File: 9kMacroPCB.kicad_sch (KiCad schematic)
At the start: 0 parts

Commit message: PCB updates
added PCB device libs and assigned footprints
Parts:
- added D1, D2, D3, D4, D5, D6, D7, D8, D9: D_Small, Diode_SMD:D_SOD-123, symbol Device:D_Small
- added MX1, MX2, MX3, MX4, MX5, MX6, MX7, MX8, MX9: MX-NoLED, MX_Alps_Hybrid2:MX-1U-NoLED, symbol MX_Alps_Hybrid:MX-NoLED
- added R1, R2, R3, R4, R5, R6: 10k, Resistor_SMD:R_0805_2012Metric, symbol Device:R_Small
- added U1: XIAO-RP2040-SMD, Seeed Studio XIAO Series Library:XIAO-RP2040-DIP, symbol Seeed_Studio_XIAO_Series:XIAO-RP2040-SMD
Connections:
- new net: D9.2 (A), MX9.2 (ROW)
- new net: R6.2, U1.6 (GPIO7_D5_SCL)
- new net: D4.2 (A), MX8.2 (ROW)
- new net: R4.2, U1.4 (GPIO29_A3_D3)
- new net: R1.2, U1.1 (GPIO26_A0_D0)
- new net: R2.2, U1.2 (GPIO27_A1_D1)
- new net: R3.2, U1.3 (GPIO28_A2_D2)
- new net: R5.2, U1.5 (GPIO6_D4_SDA)
- new net: D7.2 (A), MX3.2 (ROW)
- new net: D2.2 (A), MX4.2 (ROW)
- new net: D1.2 (A), MX1.2 (ROW)
- new net: D8.2 (A), MX6.2 (ROW)
- new net: D3.2 (A), MX7.2 (ROW)
- new net: D6.2 (A), MX2.2 (ROW)
- new net: D5.2 (A), MX5.2 (ROW)
- new net COL0: MX1.1 (COL), MX4.1 (COL), MX7.1 (COL)
- new net COL1: MX2.1 (COL), MX5.1 (COL), MX8.1 (COL)
- new net COL2: MX3.1 (COL), MX6.1 (COL), MX9.1 (COL)
- new net ROW0: D1.1 (K), D6.1 (K), D7.1 (K)
- new net ROW1: D2.1 (K), D5.1 (K), D8.1 (K)
- new net ROW2: D3.1 (K), D4.1 (K), D9.1 (K)

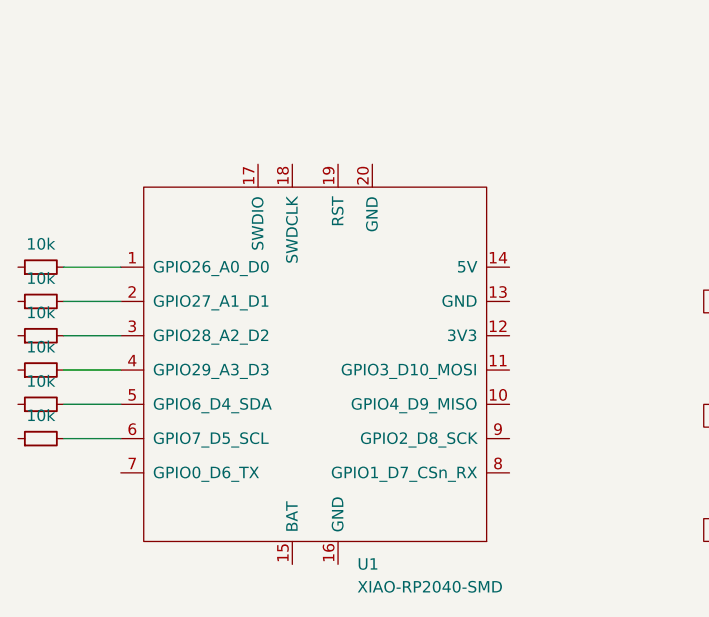
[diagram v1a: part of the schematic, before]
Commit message: Remove OPL library, add XIAO RP2040 library, update schematic
Removed the OPL_Kicad_Library submodule and added Seeeduino XIAO RP2040 KiCAD symbol and footprint libraries. Updated 9kMacroPCB.kicad_sch to remove R_Small resistors and references to the OPL library, and adjusted the schematic to use the new XIAO RP2040 symbols. Updated fp-lib-table and sym-lib-table accordingly. Added new backup files and lock files.
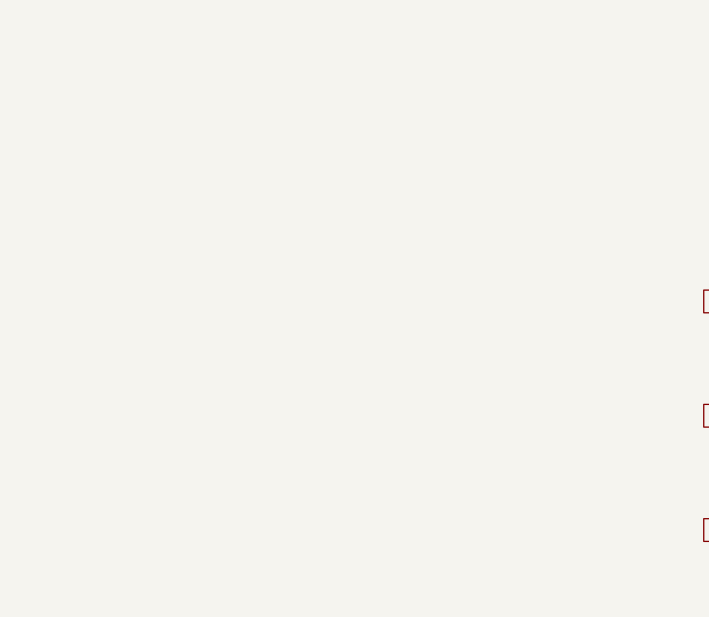
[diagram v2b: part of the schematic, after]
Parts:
- removed R1, R2, R3, R4, R5, R6: 10k, Resistor_SMD:R_0805_2012Metric, symbol Device:R_Small
- removed U1: XIAO-RP2040-SMD, Seeed Studio XIAO Series Library:XIAO-RP2040-DIP, symbol Seeed_Studio_XIAO_Series:XIAO-RP2040-SMD

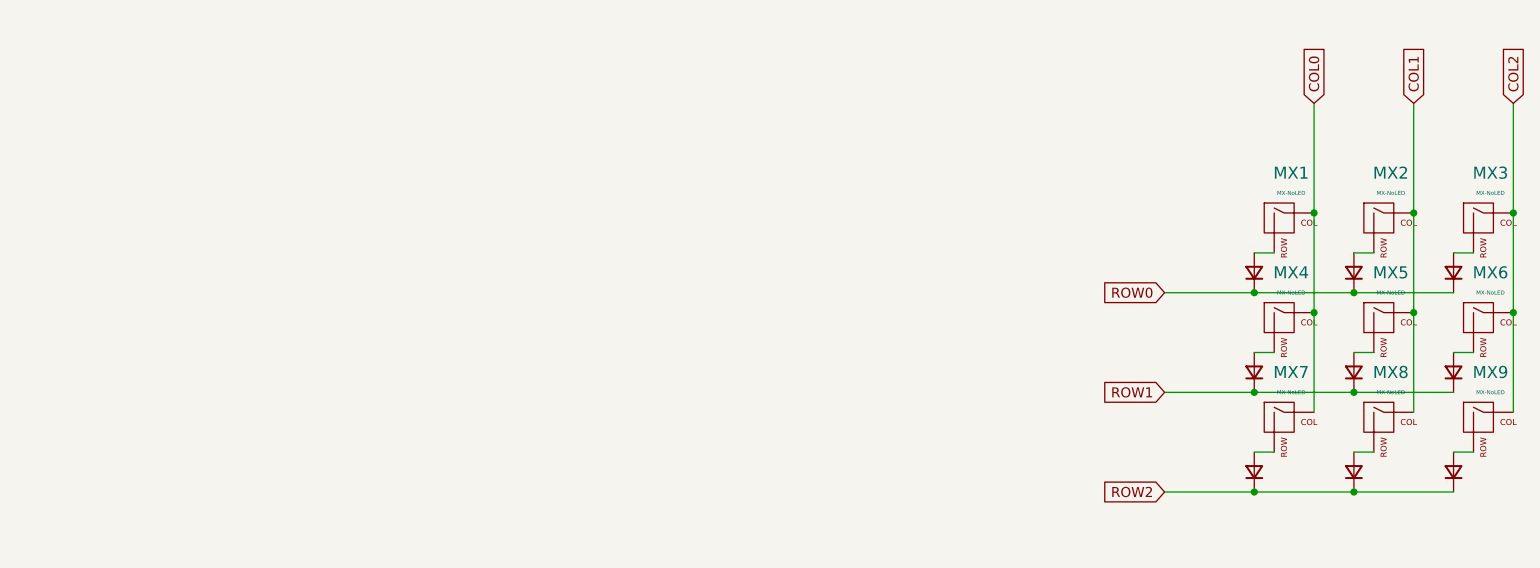
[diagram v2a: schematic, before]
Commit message: Update PCB: netlist, footprints, and backup cleanup
Removed old backup zip files and added an auto-saved file reference. Updated net assignments and pin naming in 9kMacroPCB.kicad_pcb, made significant changes to footprints (notably D1, R4, and U1), and adjusted component placements and net connections. These changes reflect schematic and layout updates for improved accuracy and maintainability.
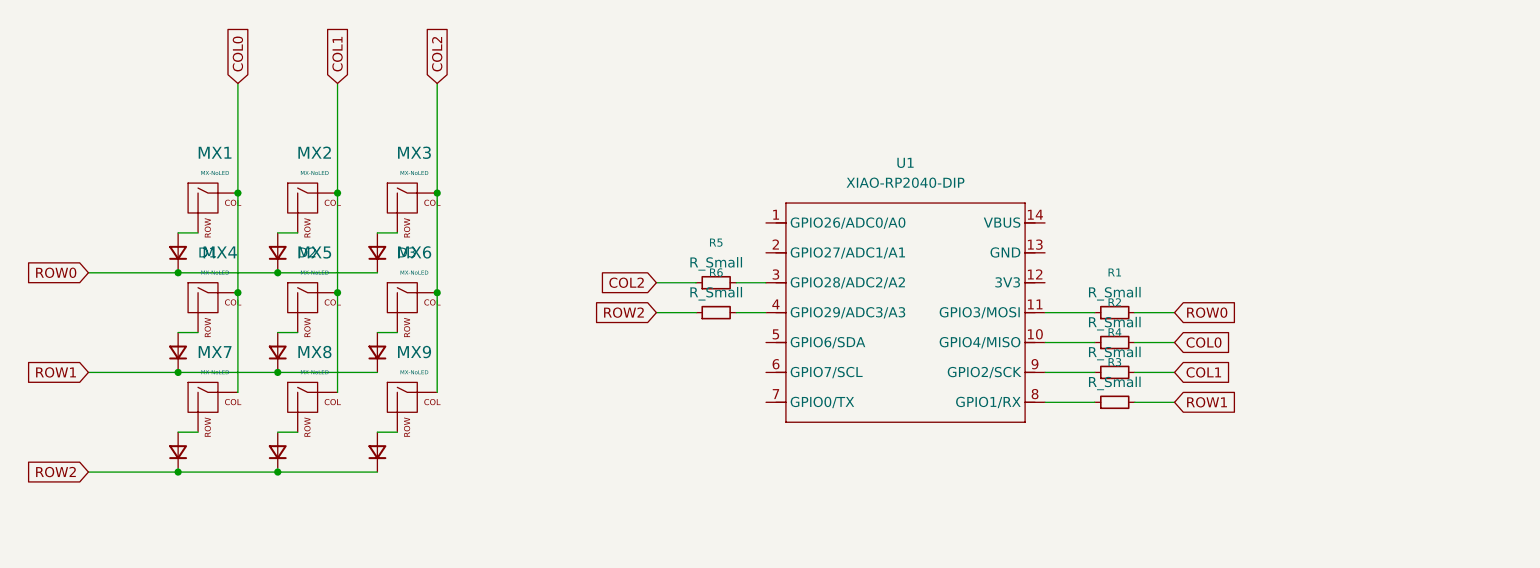
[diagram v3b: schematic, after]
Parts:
- added R1, R2, R3, R4, R5, R6: R_Small, Resistor_SMD:R_0805_2012Metric, symbol Device:R_Small
- added U1: XIAO-RP2040-DIP, XIAO_PCB:XIAO-RP2040-DIP, symbol Seeed_Studio_XIAO_Series:XIAO-RP2040-DIP
- renumbered D6 to D2, D7 to D3, D2 to D4, D8 to D6, D3 to D7, D4 to D8
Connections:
- net COL0: now also R2.2
- net COL1: now also R4.2
- net COL2: now also R5.1
- net ROW0: now also R1.2
- net ROW1: now also R3.2
- net ROW2: now also R6.1
- new net: R6.2, U1.4 (GPIO29/ADC3/A3)
- new net: R2.1, U1.10 (GPIO4/MISO)
- new net: R1.1, U1.11 (GPIO3/MOSI)
- new net: R5.2, U1.3 (GPIO28/ADC2/A2)
- new net: R3.1, U1.8 (GPIO1/RX)
- new net: R4.1, U1.9 (GPIO2/SCK)
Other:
- moved on the sheet: MX1, MX2, MX3, MX4, MX5, MX6, MX7, MX8, MX9
